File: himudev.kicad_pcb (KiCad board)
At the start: 4 copper layers, 93.6 x 43.6 mm, 132 parts, among them J1 M20-8770642R, J2 USB_C16PIN, J3 M20-8770642R, J4 20021121-00010C4LF, J5 M20-8762042, Q1 IRLML6402, Q2 BSS214NW, Q3 BSS214NW, Q4 BSS214NW, Q5 BSS214NW, Q6 BSS214NW, U1 FT230XS, U2 MCP1726-3302ESN, U3 MIC5319-1.8YD5-TR, U4 IS25WP032D, U5 FE310-G002, U6 ICM-20948, U7 BMP388, X1 KX2132709Z, Y1 TSX-3225 16.0000MF18X-AC0

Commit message: Add board cutouts (enclosure features)
Also, more placement of the components done.
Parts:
- moved U1 179.8 mm to (126.0, 101.6), turned to 90 degrees
- moved D9 135.1 mm to (139.6, 120.8)
- moved R27 135.1 mm to (140.3, 117.5)
- moved S1 135.1 mm to (146.9, 119.2)
- moved TP6 135.0 mm to (90.2, 128.5)
- moved C6 134.9 mm to (92.8, 99.5)
- moved C9 134.9 mm to (79.9, 88.5)
- moved D3 134.9 mm to (93.9, 90.5)
- moved D4 134.9 mm to (88.5, 95.0)
- moved R14 134.9 mm to (88.9, 99.4)
- moved R18 134.9 mm to (74.3, 109.1)
- moved R20 134.9 mm to (94.0, 114.7)
- moved C11 134.9 mm to (93.1, 111.4)
- moved C3 134.9 mm to (83.9, 103.2)
- moved C5 134.9 mm to (79.1, 106.0)
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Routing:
- net /MCU_clk_reset/GPIO_0: track 0.00 -> 25.1 mm
- net /MCU_clk_reset/SPI_CS0: track 0.00 -> 22.7 mm
- net /MCU_clk_reset/GPIO_1: track 0.00 -> 17.4 mm
- net +5V: track 60.4 -> 77.8 mm, vias 1 -> 3
- net /MCU_clk_reset/SPI_MOSI: track 0.00 -> 16.0 mm
- net Net-(R12-Pad1): track 0.00 -> 11.8 mm
- net Net-(R13-Pad1): track 0.00 -> 11.8 mm
- net GND: track 42.3 -> 53.1 mm, vias 11 -> 14
- net Net-(R15-Pad2): track 0.00 -> 5.24 mm
- net +3V3: track 12.4 -> 16.1 mm
- net Net-(C8-Pad1): track 0.00 -> 3.02 mm
- net Net-(TP9-Pad1): track 2.57 -> 0.02 mm
- net VBUS: track 85.5 -> 87.2 mm
- net VINP: track 84.5 -> 85.2 mm
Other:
- outline, holes or cut-outs redrawn

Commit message: Remap main header pins
Allows for better use of board estate.
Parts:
- moved C22 299.1 mm to (174.6, 114.2), turned to 270 degrees
- moved R40 257.7 mm to (160.5, 92.6), turned to 0 degrees
- moved R42 254.8 mm to (160.5, 89.2), turned to 0 degrees
- moved D11 253.4 mm to (164.6, 92.6), turned to 180 degrees
- moved Q3 252.5 mm to (172.2, 96.3), turned to 180 degrees
- moved R44 252.1 mm to (160.5, 85.7), turned to 0 degrees
- moved D12 250.5 mm to (164.6, 89.2), turned to 180 degrees
- moved Q4 249.5 mm to (172.2, 92.8), turned to 180 degrees
- moved R46 249.1 mm to (160.5, 82.3), turned to 0 degrees
- moved R39 247.4 mm to (176.0, 96.3), turned to 0 degrees
- moved D13 247.4 mm to (164.6, 85.7), turned to 180 degrees
- moved Q5 245.7 mm to (172.2, 89.4), turned to 180 degrees
- moved D14 243.9 mm to (164.6, 82.3), turned to 180 degrees
- moved R41 243.9 mm to (176.0, 92.7), turned to 0 degrees
- moved Q6 242.6 mm to (169.3, 85.7), turned to 180 degrees
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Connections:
- net Net-(R29-Pad1) renamed /MCU_clk_reset/QSPI_CS
- net Net-(R30-Pad2) renamed /MCU_clk_reset/QSPI_3
- net Net-(U4-Pad2) renamed /MCU_clk_reset/QSPI_1
- net Net-(U4-Pad3) renamed /MCU_clk_reset/QSPI_2
- net Net-(U4-Pad5) renamed /MCU_clk_reset/QSPI_0
- net Net-(U4-Pad6) renamed /MCU_clk_reset/QSPI_SCK
- J5 pad 10: /MCU_clk_reset/nRESET -> /MCU_clk_reset/GPIO_23
- J5 pad 11: /MCU_clk_reset/VDD_CORE_EN -> /MCU_clk_reset/GPIO_20
- J5 pad 12: /MCU_clk_reset/PMU_OUT_1 -> /MCU_clk_reset/GPIO_21
- J5 pad 14: /MCU_clk_reset/GPIO_23 -> /MCU_clk_reset/GPIO_19
- J5 pad 15: /MCU_clk_reset/GPIO_22 -> /MCU_clk_reset/GPIO_18
- J5 pad 16: /MCU_clk_reset/GPIO_21 -> /MCU_clk_reset/GPIO_17
- J5 pad 17: /MCU_clk_reset/GPIO_20 -> /MCU_clk_reset/GPIO_16
- J5 pad 18: /MCU_clk_reset/GPIO_19 -> /MCU_clk_reset/I2C_SCL
- J5 pad 19: /MCU_clk_reset/GPIO_18 -> /MCU_clk_reset/I2C_SDA
- J5 pad 20: /MCU_clk_reset/GPIO_17 -> /MCU_clk_reset/I2C_INT
- J5 pad 21: /MCU_clk_reset/GPIO_16 -> /MCU_clk_reset/SPI_FSYNC
- J5 pad 22: /MCU_clk_reset/I2C_SCL -> /MCU_clk_reset/SPI_INT
- J5 pad 23: /MCU_clk_reset/I2C_SDA -> /MCU_clk_reset/SPI_SCK
- J5 pad 24: /MCU_clk_reset/I2C_INT -> /MCU_clk_reset/SPI_MISO
- J5 pad 25: /MCU_clk_reset/SPI_FSYNC -> /MCU_clk_reset/SPI_MOSI
- J5 pad 26: /MCU_clk_reset/SPI_INT -> /MCU_clk_reset/SPI_CS0
- J5 pad 27: /MCU_clk_reset/SPI_SCK -> /MCU_clk_reset/GPIO_1
- J5 pad 28: /MCU_clk_reset/SPI_MISO -> /MCU_clk_reset/GPIO_0
- J5 pad 29: /MCU_clk_reset/SPI_MOSI -> /MCU_clk_reset/nRESET
- J5 pad 30: /MCU_clk_reset/SPI_CS0 -> /MCU_clk_reset/VDD_CORE_EN
- J5 pad 31: /MCU_clk_reset/GPIO_1 -> /MCU_clk_reset/WAKE
- J5 pad 32: /MCU_clk_reset/GPIO_0 -> /MCU_clk_reset/PMU_OUT_1
- J5 pad 9: /MCU_clk_reset/WAKE -> /MCU_clk_reset/GPIO_22
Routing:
- net GND: track 53.1 -> 78.5 mm, vias 14 -> 22
- net +3V3: track 16.1 -> 37.5 mm, vias 1 -> 8
- net /MCU_clk_reset/GPIO_0: track 25.1 -> 7.94 mm
- net /MCU_clk_reset/I2C_INT: track 6.11 -> 22.0 mm
- net /MCU_clk_reset/I2C_SCL: track 5.26 -> 20.8 mm
- net /MCU_clk_reset/GPIO_1: track 17.4 -> 1.92 mm
- net /MCU_clk_reset/SPI_CS0: track 22.7 -> 7.94 mm
- net /MCU_clk_reset/SPI_MOSI: track 16.0 -> 1.92 mm
- net Net-(D5-Pad1): track 0.00 -> 13.5 mm
- net Net-(R12-Pad1): track 11.8 -> 1.08 mm
- net Net-(R13-Pad1): track 11.8 -> 1.08 mm
- net /MCU_clk_reset/VDD_CORE_EN: track 0.00 -> 10.6 mm
- net /MCU_clk_reset/GPIO_17: track 0.00 -> 7.95 mm
- net /MCU_clk_reset/GPIO_23: track 0.00 -> 7.94 mm
- net /MCU_clk_reset/GPIO_21: track 0.00 -> 7.94 mm
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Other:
- net class Default: clearance 0.254 -> 0.127; via_dia 0.508 -> 0.635; via_drill 0.254 -> 0.3
- rule trace_clearance: 0.254 -> 0.127

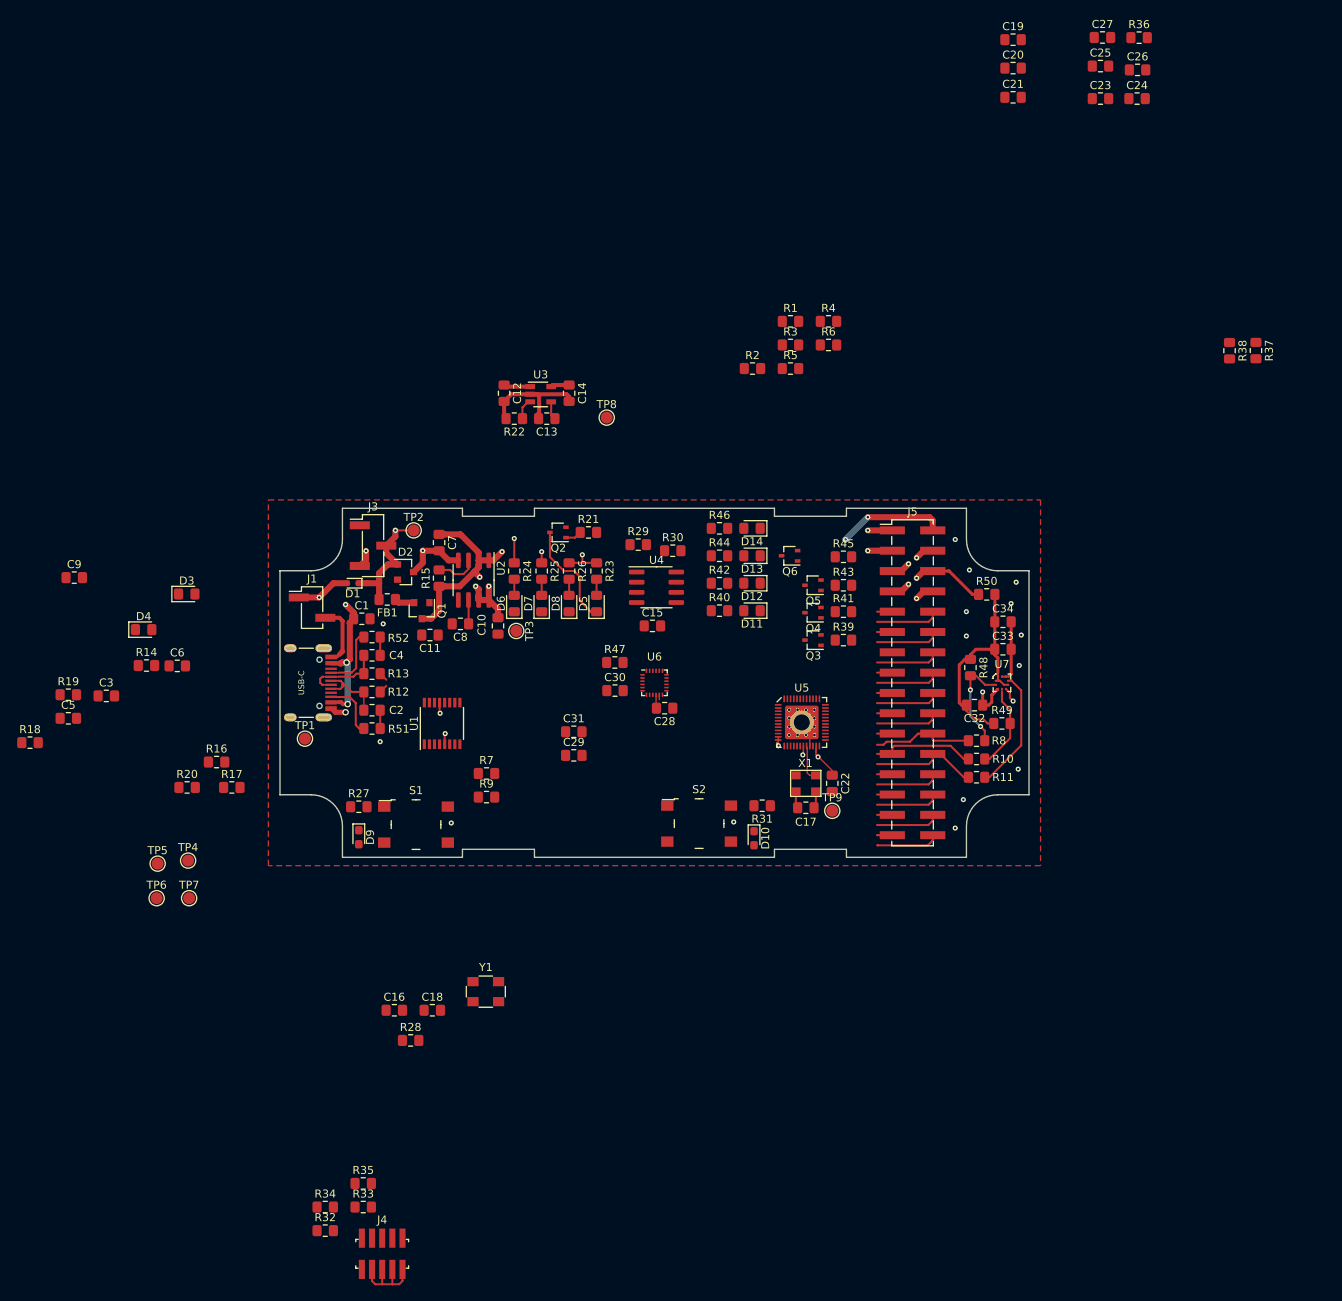
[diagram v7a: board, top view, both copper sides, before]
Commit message: Use 0603 components, on both sides, route header
This decision was due to the current placement overcrowded and to the
fact that successful routing on one side was uncertain.
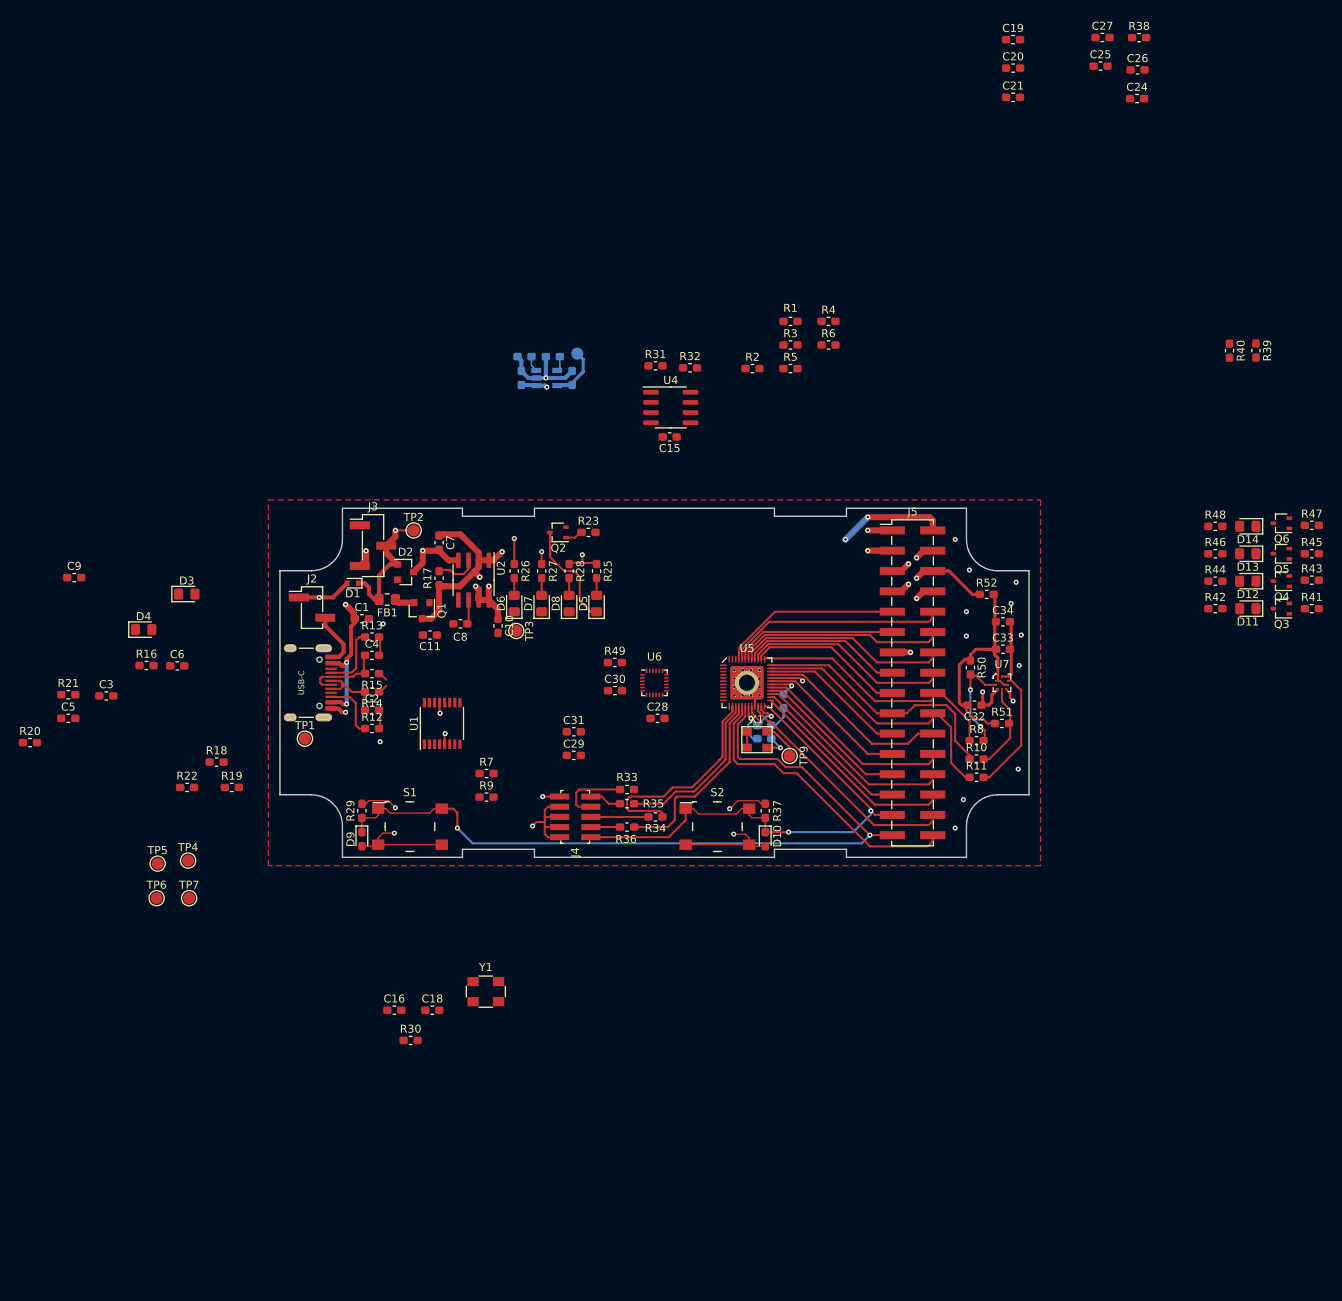
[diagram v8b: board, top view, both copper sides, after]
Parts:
- C1, C10, C11, C15, C16, C18, C19, C2, C20, C21, C24, C25, C26, C27, C28, C29, C3, C30, C31, C32, C33, C34, C4, C5, C6, C7, C8, C9: footprint Capacitor_SMD:C_0805_2012Metric_Pad1.15x1.40mm_HandSolder -> Capacitor_SMD:C_0603_1608Metric_Pad1.05x0.95mm_HandSolder
- C12, C13, C14, C17, C22, C23: footprint Capacitor_SMD:C_0805_2012Metric_Pad1.15x1.40mm_HandSolder -> Capacitor_SMD:C_0603_1608Metric_Pad1.05x0.95mm_HandSolder; moved to B.Cu
- R1, R10, R11, R2, R29, R3, R31, R33, R34, R35, R36, R38, R39, R4, R41, R42, R43, R44, R45, R46, R5, R6, R7, R8, R9: footprint Resistor_SMD:R_0805_2012Metric_Pad1.15x1.40mm_HandSolder -> Resistor_SMD:R_0603_1608Metric_Pad1.05x0.95mm_HandSolder
- R12, R13: value 27 -> 5k1; footprint Resistor_SMD:R_0805_2012Metric_Pad1.15x1.40mm_HandSolder -> Resistor_SMD:R_0603_1608Metric_Pad1.05x0.95mm_HandSolder
- R14, R15: value 10k -> 27; footprint Resistor_SMD:R_0805_2012Metric_Pad1.15x1.40mm_HandSolder -> Resistor_SMD:R_0603_1608Metric_Pad1.05x0.95mm_HandSolder
- R16: value 100k -> 10k; footprint Resistor_SMD:R_0805_2012Metric_Pad1.15x1.40mm_HandSolder -> Resistor_SMD:R_0603_1608Metric_Pad1.05x0.95mm_HandSolder
- R17: value 1k -> 10k; footprint Resistor_SMD:R_0805_2012Metric_Pad1.15x1.40mm_HandSolder -> Resistor_SMD:R_0603_1608Metric_Pad1.05x0.95mm_HandSolder
- R18: value 270 -> 100k; footprint Resistor_SMD:R_0805_2012Metric_Pad1.15x1.40mm_HandSolder -> Resistor_SMD:R_0603_1608Metric_Pad1.05x0.95mm_HandSolder
- R19: value 270 -> 1k; footprint Resistor_SMD:R_0805_2012Metric_Pad1.15x1.40mm_HandSolder -> Resistor_SMD:R_0603_1608Metric_Pad1.05x0.95mm_HandSolder
- R20: value 100k -> 270; footprint Resistor_SMD:R_0805_2012Metric_Pad1.15x1.40mm_HandSolder -> Resistor_SMD:R_0603_1608Metric_Pad1.05x0.95mm_HandSolder
- R21: value 100 -> 270; footprint Resistor_SMD:R_0805_2012Metric_Pad1.15x1.40mm_HandSolder -> Resistor_SMD:R_0603_1608Metric_Pad1.05x0.95mm_HandSolder
- R22: value 10k -> 100k; footprint Resistor_SMD:R_0805_2012Metric_Pad1.15x1.40mm_HandSolder -> Resistor_SMD:R_0603_1608Metric_Pad1.05x0.95mm_HandSolder
- R23, R40: value 270 -> 100; footprint Resistor_SMD:R_0805_2012Metric_Pad1.15x1.40mm_HandSolder -> Resistor_SMD:R_0603_1608Metric_Pad1.05x0.95mm_HandSolder
- R24: value 560 -> 10k; footprint Resistor_SMD:R_0805_2012Metric_Pad1.15x1.40mm_HandSolder -> Resistor_SMD:R_0603_1608Metric_Pad1.05x0.95mm_HandSolder; moved to B.Cu
- R25: value 560 -> 270; footprint Resistor_SMD:R_0805_2012Metric_Pad1.15x1.40mm_HandSolder -> Resistor_SMD:R_0603_1608Metric_Pad1.05x0.95mm_HandSolder
- R26: value 270 -> 560; footprint Resistor_SMD:R_0805_2012Metric_Pad1.15x1.40mm_HandSolder -> Resistor_SMD:R_0603_1608Metric_Pad1.05x0.95mm_HandSolder
- R27: value 100k -> 560; footprint Resistor_SMD:R_0805_2012Metric_Pad1.15x1.40mm_HandSolder -> Resistor_SMD:R_0603_1608Metric_Pad1.05x0.95mm_HandSolder
- R28: value 1M -> 270; footprint Resistor_SMD:R_0805_2012Metric_Pad1.15x1.40mm_HandSolder -> Resistor_SMD:R_0603_1608Metric_Pad1.05x0.95mm_HandSolder
- R30: value 100k -> 1M; footprint Resistor_SMD:R_0805_2012Metric_Pad1.15x1.40mm_HandSolder -> Resistor_SMD:R_0603_1608Metric_Pad1.05x0.95mm_HandSolder
- R32, R37: value 100 -> 100k; footprint Resistor_SMD:R_0805_2012Metric_Pad1.15x1.40mm_HandSolder -> Resistor_SMD:R_0603_1608Metric_Pad1.05x0.95mm_HandSolder
- R47: value 0 -> 100; footprint Resistor_SMD:R_0805_2012Metric_Pad1.15x1.40mm_HandSolder -> Resistor_SMD:R_0603_1608Metric_Pad1.05x0.95mm_HandSolder
- R48: value 4k7 -> 270; footprint Resistor_SMD:R_0805_2012Metric_Pad1.15x1.40mm_HandSolder -> Resistor_SMD:R_0603_1608Metric_Pad1.05x0.95mm_HandSolder
- R49: value 4k7 -> 0; footprint Resistor_SMD:R_0805_2012Metric_Pad1.15x1.40mm_HandSolder -> Resistor_SMD:R_0603_1608Metric_Pad1.05x0.95mm_HandSolder
- R50: value 0 -> 4k7; footprint Resistor_SMD:R_0805_2012Metric_Pad1.15x1.40mm_HandSolder -> Resistor_SMD:R_0603_1608Metric_Pad1.05x0.95mm_HandSolder
- R51: value 5k1 -> 4k7; footprint Resistor_SMD:R_0805_2012Metric_Pad1.15x1.40mm_HandSolder -> Resistor_SMD:R_0603_1608Metric_Pad1.05x0.95mm_HandSolder
- R52: value 5k1 -> 0; footprint Resistor_SMD:R_0805_2012Metric_Pad1.15x1.40mm_HandSolder -> Resistor_SMD:R_0603_1608Metric_Pad1.05x0.95mm_HandSolder
- TP8, U3: moved to B.Cu
- moved R36 117.6 mm to (149.0, 119.6), turned to 180 degrees
- moved R32 117.1 mm to (156.8, 62.2)
- moved R47 88.8 mm to (234.6, 81.9)
- moved C23 85.1 mm to (168.5, 103.9), turned to 270 degrees
- moved R37 84.1 mm to (166.2, 117.6)
- moved R51 78.7 mm to (195.8, 106.7)
- moved R52 77.0 mm to (193.9, 90.6)
- moved R40 71.6 mm to (224.3, 60.1), turned to 270 degrees
- moved R30 69.4 mm to (121.9, 146.3)
- moved R21 68.1 mm to (79.1, 103.1)
- moved R34 63.9 mm to (152.5, 118.4), turned to 180 degrees
- moved R39 63.0 mm to (227.6, 60.1), turned to 270 degrees
- moved R42 62.1 mm to (222.5, 92.3)
- moved R44 62.1 mm to (222.5, 88.9)
- moved R46 62.1 mm to (222.5, 85.5)
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- renumbered J2 to J1, J1 to J2
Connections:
- J1 pad A5: Net-(J2-PadA5) -> Net-(J1-PadA5)
- J1 pad B5: Net-(J2-PadB5) -> Net-(J1-PadB5)
- J5 pad 10: /MCU_clk_reset/GPIO_23 -> /MCU_clk_reset/GPIO_22
- J5 pad 11: /MCU_clk_reset/GPIO_20 -> /MCU_clk_reset/GPIO_21
- J5 pad 12: /MCU_clk_reset/GPIO_21 -> /MCU_clk_reset/GPIO_20
- J5 pad 9: /MCU_clk_reset/GPIO_22 -> /MCU_clk_reset/GPIO_23
- R12 pad 1: Net-(R12-Pad1) -> Net-(J1-PadB5)
- R12 pad 2: /USB_Power/USB_D+ -> GND
- R13 pad 1: Net-(R13-Pad1) -> Net-(J1-PadA5)
- R13 pad 2: /USB_Power/USB_D- -> GND
- R14 pad 1: Net-(C3-Pad1) -> Net-(R14-Pad1)
- R14 pad 2: Net-(C6-Pad1) -> /USB_Power/USB_D+
- R15 pad 1: +5V -> Net-(R15-Pad1)
- R15 pad 2: Net-(R15-Pad2) -> /USB_Power/USB_D-
- R16 pad 2: Net-(C11-Pad2) -> Net-(C6-Pad1)
- R17 pad 1: Net-(C11-Pad2) -> +5V
- R17 pad 2: /USB_Power/PWREN# -> Net-(R17-Pad2)
- R18 pad 1: Net-(C9-Pad1) -> Net-(C3-Pad1)
- R18 pad 2: Net-(D3-Pad2) -> Net-(C11-Pad2)
- R19 pad 1: Net-(C9-Pad1) -> Net-(C11-Pad2)
- R19 pad 2: Net-(D4-Pad2) -> /USB_Power/PWREN#
- R20 pad 1: +5V -> Net-(C9-Pad1)
- R20 pad 2: Net-(C11-Pad2) -> Net-(D3-Pad2)
- R21 pad 1: Net-(Q2-Pad1) -> Net-(C9-Pad1)
- R21 pad 2: +1V8 -> Net-(D4-Pad2)
- R22 pad 1: /MCU_clk_reset/VDD_CORE_EN -> +5V
- R22 pad 2: GND -> Net-(C11-Pad2)
- R23 pad 1: +3V3 -> Net-(Q2-Pad1)
- R23 pad 2: Net-(D5-Pad2) -> +1V8
- R24 pad 1: VBUS -> /MCU_clk_reset/VDD_CORE_EN
- R24 pad 2: Net-(D6-Pad2) -> GND
- R25 pad 1: +5V -> +3V3
- R25 pad 2: Net-(D7-Pad2) -> Net-(D5-Pad2)
- R26 pad 1: +3V3 -> VBUS
- R26 pad 2: Net-(D8-Pad2) -> Net-(D6-Pad2)
- R27 pad 1: +3V3 -> +5V
- R27 pad 2: /MCU_clk_reset/WAKE -> Net-(D7-Pad2)
- R28 pad 1: Net-(C18-Pad1) -> +3V3
- R28 pad 2: Net-(C16-Pad1) -> Net-(D8-Pad2)
- R29 pad 1: /MCU_clk_reset/QSPI_CS -> +3V3
- R29 pad 2: +3V3 -> /MCU_clk_reset/WAKE
- R30 pad 1: +3V3 -> Net-(C18-Pad1)
- R30 pad 2: /MCU_clk_reset/QSPI_3 -> Net-(C16-Pad1)
- R31 pad 1: +3V3 -> /MCU_clk_reset/QSPI_CS
- R31 pad 2: /MCU_clk_reset/nRESET -> +3V3
- R32 pad 1: Net-(R32-Pad1) -> +3V3
- R32 pad 2: /MCU_clk_reset/JTAG_TCK -> /MCU_clk_reset/QSPI_3
- R33 pad 2: /MCU_clk_reset/JTAG_TDO -> /MCU_clk_reset/JTAG_TCK
- R34 pad 2: /MCU_clk_reset/JTAG_TMS -> /MCU_clk_reset/JTAG_TDO
- R35 pad 2: /MCU_clk_reset/JTAG_TDI -> /MCU_clk_reset/JTAG_TMS
- R36 pad 1: +1V8 -> Net-(R36-Pad1)
- R36 pad 2: Net-(C24-Pad1) -> /MCU_clk_reset/JTAG_TDI
- R37 pad 1: /MCU_clk_reset/CONSOLE_RX -> +3V3
- R37 pad 2: /MCU_clk_reset/GPIO_16 -> /MCU_clk_reset/nRESET
- R38 pad 1: /MCU_clk_reset/CONSOLE_TX -> +1V8
- R38 pad 2: /MCU_clk_reset/GPIO_17 -> Net-(C24-Pad1)
- R39 pad 1: Net-(Q3-Pad1) -> /MCU_clk_reset/CONSOLE_RX
- R39 pad 2: /MCU_clk_reset/GPIO_20 -> /MCU_clk_reset/GPIO_16
- R40 pad 1: +3V3 -> /MCU_clk_reset/CONSOLE_TX
- R40 pad 2: Net-(D11-Pad2) -> /MCU_clk_reset/GPIO_17
- R41 pad 1: Net-(Q4-Pad1) -> Net-(Q3-Pad1)
- R41 pad 2: /MCU_clk_reset/GPIO_19 -> /MCU_clk_reset/GPIO_20
- R42 pad 2: Net-(D12-Pad2) -> Net-(D11-Pad2)
- R43 pad 1: Net-(Q5-Pad1) -> Net-(Q4-Pad1)
- R43 pad 2: /MCU_clk_reset/GPIO_21 -> /MCU_clk_reset/GPIO_19
- R44 pad 2: Net-(D13-Pad2) -> Net-(D12-Pad2)
- R45 pad 1: Net-(Q6-Pad1) -> Net-(Q5-Pad1)
- R45 pad 2: /MCU_clk_reset/GPIO_22 -> /MCU_clk_reset/GPIO_21
- R46 pad 2: Net-(D14-Pad2) -> Net-(D13-Pad2)
- R47 pad 1: +3V3 -> Net-(Q6-Pad1)
- R47 pad 2: Net-(C29-Pad1) -> /MCU_clk_reset/GPIO_22
- R48 pad 1: Net-(C32-Pad2) -> +3V3
- R48 pad 2: /Sensors/BMP_SCL -> Net-(D14-Pad2)
- R49 pad 1: Net-(C32-Pad2) -> +3V3
- R49 pad 2: /Sensors/BMP_SDA -> Net-(C29-Pad1)
- R50 pad 1: +3V3 -> Net-(C32-Pad2)
- R50 pad 2: Net-(C32-Pad2) -> /Sensors/BMP_SCL
- R51 pad 1: Net-(J2-PadB5) -> Net-(C32-Pad2)
- R51 pad 2: GND -> /Sensors/BMP_SDA
- R52 pad 1: Net-(J2-PadA5) -> +3V3
- R52 pad 2: GND -> Net-(C32-Pad2)
- U1 pad 8: Net-(R12-Pad1) -> Net-(R14-Pad1)
- U1 pad 9: Net-(R13-Pad1) -> Net-(R15-Pad1)
- U2 pad 3: Net-(R15-Pad2) -> Net-(R17-Pad2)
- U5 pad 13: Net-(R32-Pad1) -> Net-(R33-Pad1)
- U5 pad 14: Net-(R33-Pad1) -> Net-(R34-Pad1)
- U5 pad 15: Net-(R34-Pad1) -> Net-(R35-Pad1)
- U5 pad 16: Net-(R35-Pad1) -> Net-(R36-Pad1)
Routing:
- net /MCU_clk_reset/WAKE: track 1.92 -> 100.1 mm, vias 0 -> 2
- net /MCU_clk_reset/nRESET: track 1.92 -> 63.8 mm, vias 0 -> 2
- net GND: track 78.5 -> 111.5 mm, vias 22 -> 28
- net /MCU_clk_reset/PMU_OUT_1: track 7.88 -> 37.5 mm
- net Net-(R34-Pad1): track 0.00 -> 27.8 mm
- net /MCU_clk_reset/SPI_MISO: track 0.00 -> 26.6 mm
- net /MCU_clk_reset/GPIO_22: track 1.92 -> 27.5 mm
- net Net-(R36-Pad1): track 0.00 -> 24.8 mm
- net /MCU_clk_reset/SPI_INT: track 0.00 -> 24.4 mm
- net /MCU_clk_reset/GPIO_20: track 1.92 -> 26.2 mm
- net /MCU_clk_reset/VDD_CORE_EN: track 10.6 -> 31.5 mm
- net Net-(R35-Pad1): track 0.00 -> 20.9 mm
- net +3V3: track 37.5 -> 56.9 mm, vias 8 -> 12
- net /MCU_clk_reset/SPI_SCK: track 0.00 -> 19.1 mm
- net /MCU_clk_reset/GPIO_0: track 7.94 -> 26.6 mm
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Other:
- rule solder_mask_min_width: 0.0889 -> 0.0508
